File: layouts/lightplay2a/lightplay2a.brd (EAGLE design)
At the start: 100.5 x 79 mm, 55 parts, among them Q0 MOSFET-NCHANNELAO3404A, Q1 MOSFET-NCHANNELAO3404A, Q10 MOSFET-NCHANNELAO3404A, Q11 MOSFET-NCHANNELAO3404A, Q2 MOSFET-NCHANNELAO3404A, Q4 MOSFET-NCHANNELAO3404A, Q5 MOSFET-NCHANNELAO3404A, Q6 MOSFET-NCHANNELAO3404A, Q7 MOSFET-NCHANNELAO3404A, Q8 MOSFET-NCHANNELAO3404A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

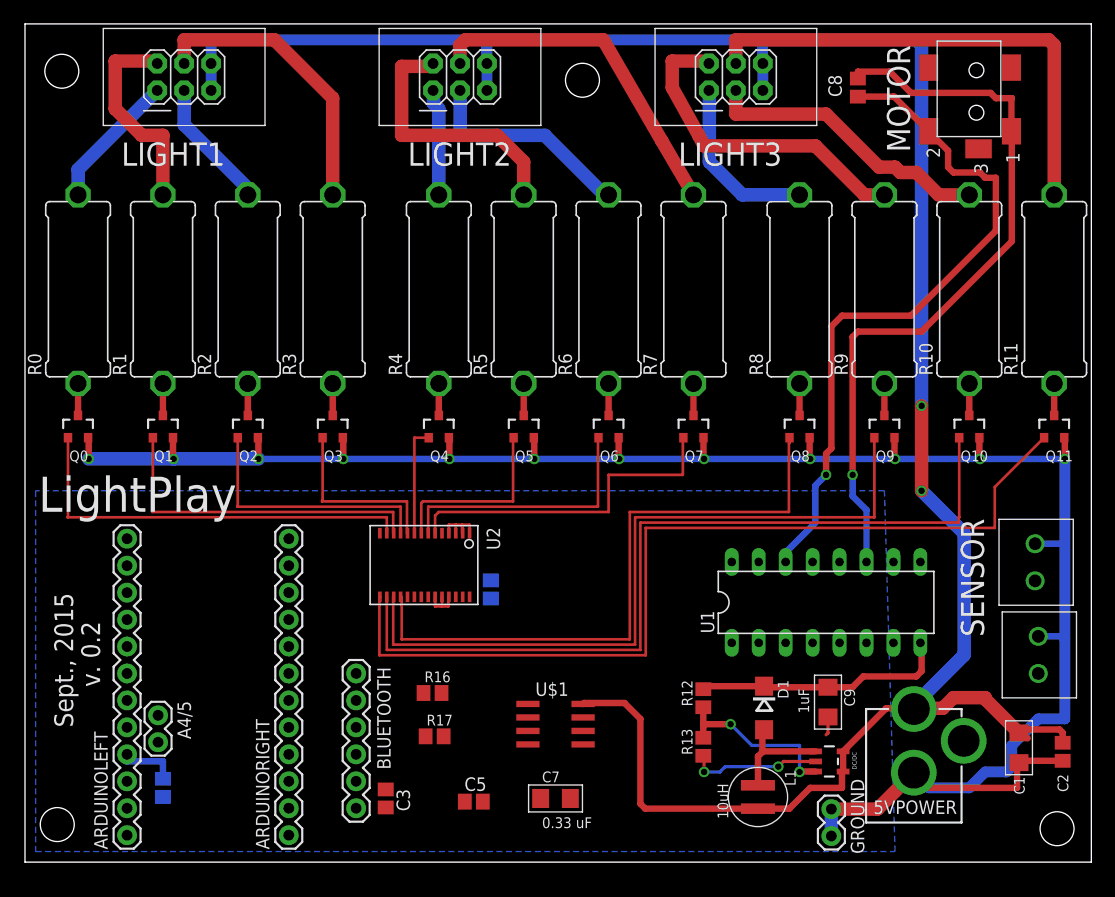
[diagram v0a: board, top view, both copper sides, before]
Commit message: working on Arduino code for LightPlay2a
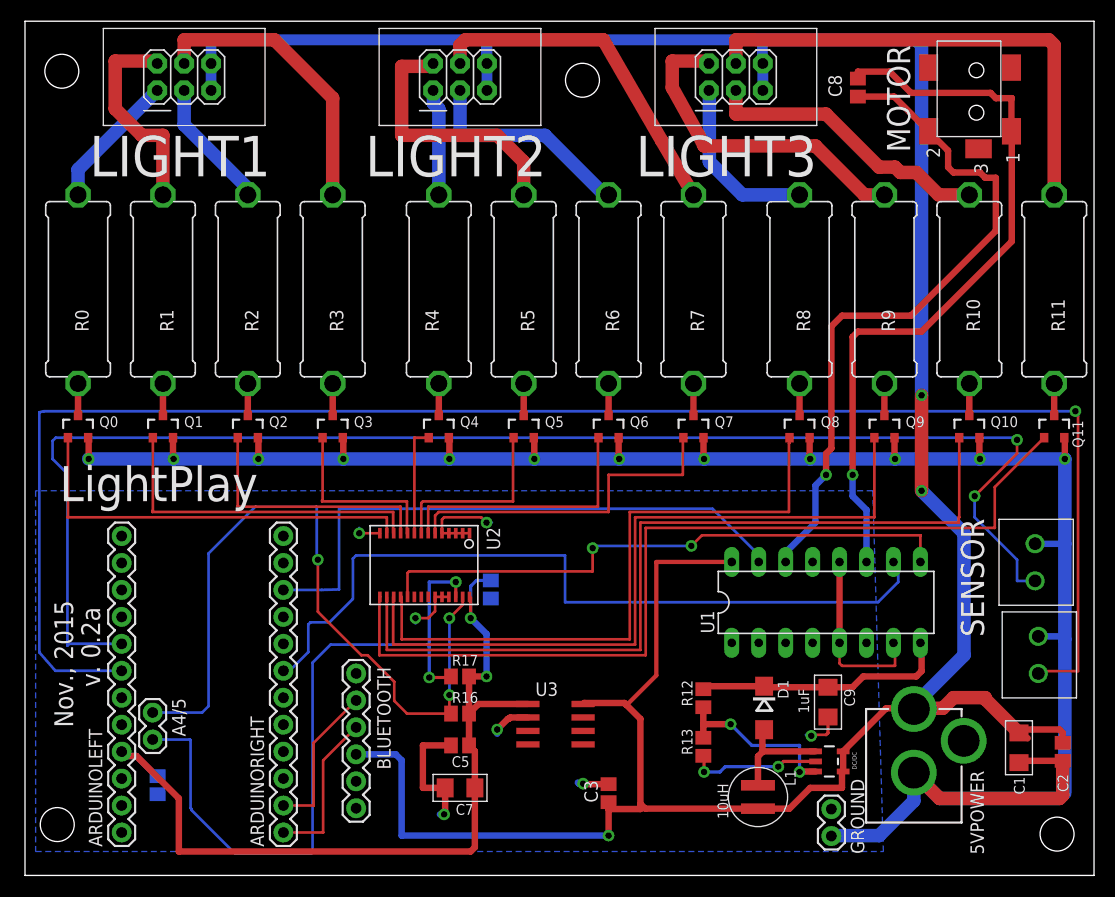
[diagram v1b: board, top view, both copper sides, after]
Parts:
- U3: value STM3.3VREG -> 3.3VREG
- moved C3 21.0 mm to (55.0, 6.50), turned to 90 degrees
- moved C7 9.06 mm to (41.0, 7.00), turned to 180 degrees
- moved R17 6.13 mm to (41.0, 17.5)
- moved C5 5.46 mm to (41.0, 11.0), turned to 180 degrees
- moved R16 3.24 mm to (41.0, 14.0)
- moved A4/5 0.57 mm to (12.0, 14.1)
- moved ARDUINOLEFT 0.57 mm to (9.11, 2.79)
- moved ARDUINORIGHT 0.57 mm to (24.4, 2.79)
- moved C6 0.57 mm to (12.5, 7.25)
- renumbered U$1 to U3
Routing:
- net A1: track 0.00 -> 157.2 mm, vias 0 -> 1
- net A0: track 0.00 -> 134.5 mm, vias 0 -> 2
- net +3V3: track 5.81 -> 81.8 mm, vias 0 -> 2
- net D4: track 0.00 -> 73.5 mm
- net SDA: track 0.00 -> 71.0 mm, vias 0 -> 3
- net SCL: track 0.00 -> 68.1 mm, vias 0 -> 2
- net +5V: track 214.5 -> 274.1 mm, vias 2 -> 3
- net D7: track 0.00 -> 56.2 mm
- net LED12: track 0.00 -> 55.9 mm, vias 0 -> 2
- net GND: track 219.0 -> 271.9 mm, vias 14 -> 21
- net N$12: track 0.00 -> 14.9 mm
- net N$11: track 0.00 -> 14.5 mm
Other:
- board size 100.5 x 79 mm -> 100.8 x 80.5 mm
- board text added: "Nov., 2015"
- board text added: "v. 0.2a"
- board text removed: "Sept., 2015"
- board text removed: "v. 0.2"

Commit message: updated Blocks documentation to include new command numbers to avoid sending '+' character to Bluetooth UART
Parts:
- C8: value 0.1uF -> TDB
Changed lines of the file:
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@@
 <attribute name="NAME" x="42.27" y="5.476" size="1.016" layer="21" font="vector" rot="R180"/>
 </element>
-<element name="C8" library="resistor" package="C0805" value="0.1uF" x="78.5" y="73" smashed="yes" rot="R90">
+<element name="C8" library="resistor" package="C0805" value="TDB" x="78.5" y="73" smashed="yes" rot="R90">
 <attribute name="NAME" x="76.984" y="72.111" size="1.27" layer="25" font="vector" rot="R90"/>
 </element>
